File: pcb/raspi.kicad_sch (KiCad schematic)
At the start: 4 parts

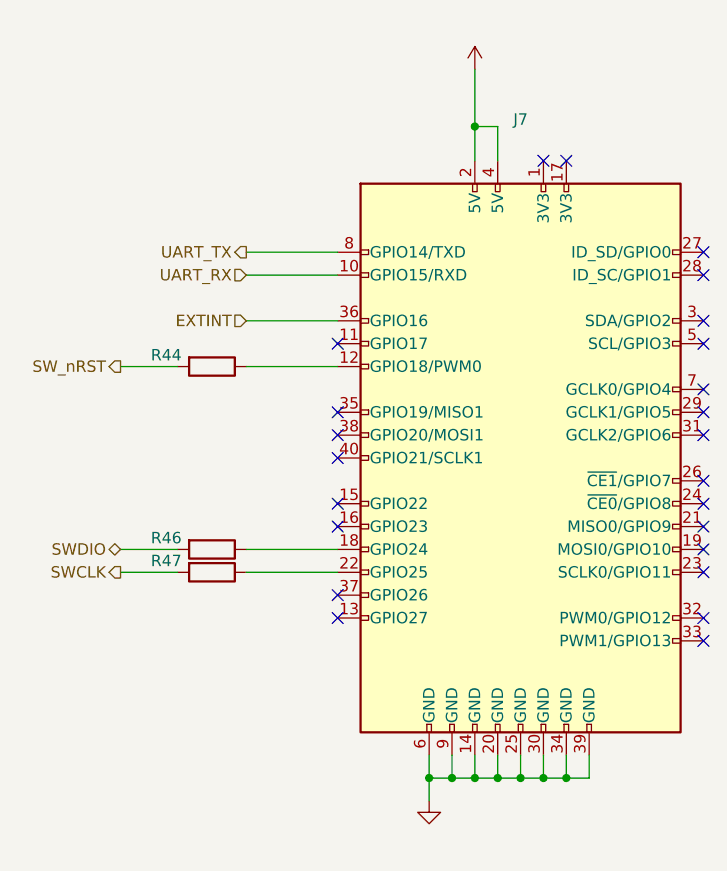
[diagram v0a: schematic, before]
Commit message: * Start replicating emonLibCM functionality
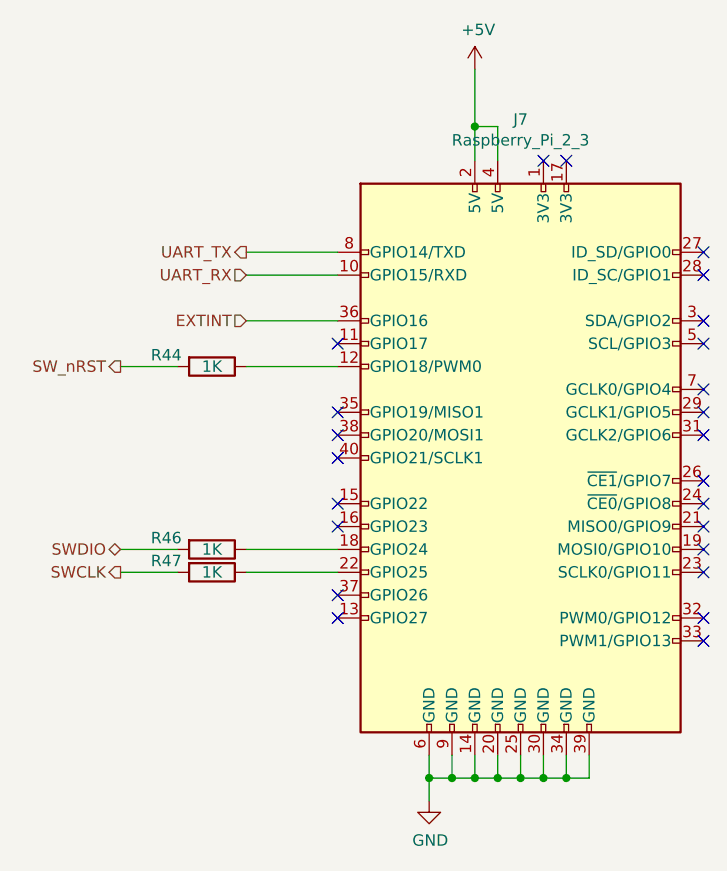
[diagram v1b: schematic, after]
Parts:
- J7: value (none) -> Raspberry_Pi_2_3; footprint (none) -> Connector_PinHeader_2.54mm:PinHeader_2x20_P2.54mm_Vertical
- R44, R46, R47: value (none) -> 1K; footprint (none) -> Resistor_SMD:R_0805_2012Metric_Pad1.20x1.40mm_HandSolder
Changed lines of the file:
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@@
     (in_bom yes) (on_board yes)
     (property "Reference" "J7" (id 0) (at 144.78 69.0626 0))
-    (property "Value" "" (id 1) (at 144.78 71.374 0))
-    (property "Footprint" "" (id 2) (at 144.78 106.68 0)
+    (property "Value" "Raspberry_Pi_2_3" (id 1) (at 144.78 71.374 0))
+    (property "Footprint" "Connector_PinHeader_2.54mm:PinHeader_2x20_P2.54mm_Vertical" (id 2) (at 144.78 106.68 0)
       (effects (font (size 1.27 1.27)) hide)
     )
@@
       (effects (font (size 1.27 1.27)) hide)
     )
-    (property "Value" "" (id 1) (at 134.747 149.1742 0))
+    (property "Value" "GND" (id 1) (at 134.747 149.1742 0))
     (property "Footprint" "" (id 2) (at 134.62 144.78 0)
       (effects (font (size 1.27 1.27)) hide)
@@
       (effects (font (size 1.27 1.27)) hide)
     )
-    (property "Value" "" (id 1) (at 140.081 59.1058 0))
+    (property "Value" "+5V" (id 1) (at 140.081 59.1058 0))
     (property "Footprint" "" (id 2) (at 139.7 63.5 0)
       (effects (font (size 1.27 1.27)) hide)
@@
     (in_bom yes) (on_board yes)
     (property "Reference" "R46" (id 0) (at 105.41 115.57 90))
-    (property "Value" "" (id 1) (at 110.49 116.84 90))
-    (property "Footprint" "" (id 2) (at 110.49 115.062 90)
+    (property "Value" "1K" (id 1) (at 110.49 116.84 90))
+    (property "Footprint" "Resistor_SMD:R_0805_2012Metric_Pad1.20x1.40mm_HandSolder" (id 2) (at 110.49 115.062 90)
       (effects (font (size 1.27 1.27)) hide)
     )
@@
     (in_bom yes) (on_board yes)
     (property "Reference" "R47" (id 0) (at 105.41 118.11 90))
-    (property "Value" "" (id 1) (at 110.49 119.38 90))
-    (property "Footprint" "" (id 2) (at 110.49 117.602 90)
+    (property "Value" "1K" (id 1) (at 110.49 119.38 90))
+    (property "Footprint" "Resistor_SMD:R_0805_2012Metric_Pad1.20x1.40mm_HandSolder" (id 2) (at 110.49 117.602 90)
       (effects (font (size 1.27 1.27)) hide)
     )
@@
     (in_bom yes) (on_board yes)
     (property "Reference" "R44" (id 0) (at 105.41 95.25 90))
-    (property "Value" "" (id 1) (at 110.49 96.52 90))
-    (property "Footprint" "" (id 2) (at 110.49 94.742 90)
+    (property "Value" "1K" (id 1) (at 110.49 96.52 90))
+    (property "Footprint" "Resistor_SMD:R_0805_2012Metric_Pad1.20x1.40mm_HandSolder" (id 2) (at 110.49 94.742 90)
       (effects (font (size 1.27 1.27)) hide)
     )
